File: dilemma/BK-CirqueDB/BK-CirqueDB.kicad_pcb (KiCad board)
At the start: 2 copper layers, 37 x 45.1 mm, 9 parts, among them J1 Conn_01x12_Female

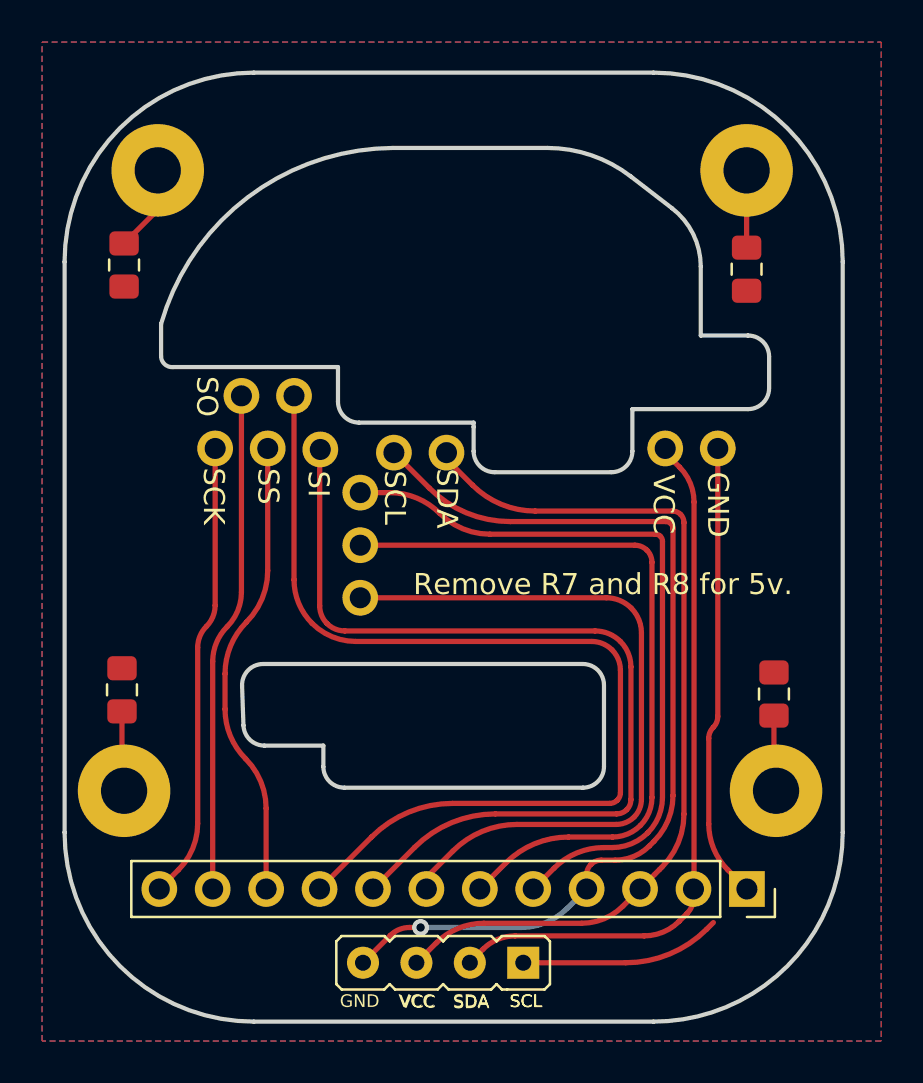
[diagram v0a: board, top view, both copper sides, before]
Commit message: make trackpad pinout compatible with oled
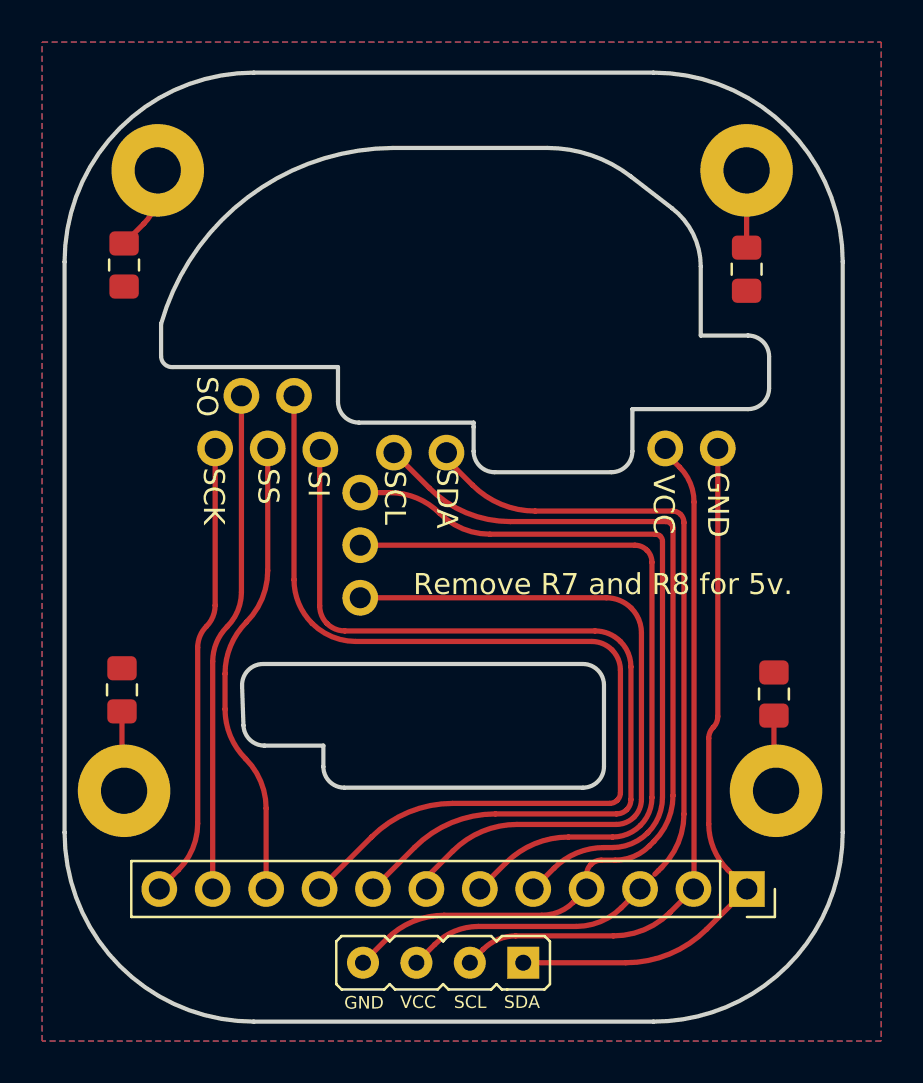
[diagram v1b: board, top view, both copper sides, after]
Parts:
- J1: value Conn_01x12_Female -> CirqueDB
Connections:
- FB1 pad 1: Net-(H1-Pad1) -> (no net)
- FB2 pad 1: Net-(H2-Pad1) -> (no net)
- FB3 pad 1: Net-(H3-Pad1) -> (no net)
- FB4 pad 1: Net-(H4-Pad1) -> (no net)
- H1 pad 1: Net-(H1-Pad1) -> Net-(FB1-Pad1)
- H2 pad 1: Net-(H2-Pad1) -> Net-(FB2-Pad1)
- H3 pad 1: Net-(H3-Pad1) -> Net-(FB3-Pad1)
- H4 pad 1: Net-(H4-Pad1) -> Net-(FB4-Pad1)
- J1 pad 1: GND -> SDA
- J1 pad 2: VCC -> SCL
- J1 pad 3: SDA -> VCC
- J1 pad 4: SCL -> GND
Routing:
- net GND: track 31.6 -> 45.9 mm
- net SCL: track 46.1 -> 33.6 mm, vias 1 -> 0
- net SDA: track 42.6 -> 33.6 mm
- net VCC: track 33.7 -> 41.6 mm
- net Net-(H2-Pad1): track 4.14 -> 0.00 mm
- net Net-(FB2-Pad1): track 0.00 -> 4.03 mm
- net Net-(H3-Pad1): track 3.82 -> 0.00 mm
- net Net-(FB3-Pad1): track 0.00 -> 3.81 mm
- net Net-(H1-Pad1): track 3.68 -> 0.00 mm
- net Net-(FB1-Pad1): track 0.00 -> 3.68 mm
- net Net-(H4-Pad1): track 3.62 -> 0.00 mm
- net Net-(FB4-Pad1): track 0.00 -> 3.61 mm
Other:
- board text added: "GND"
